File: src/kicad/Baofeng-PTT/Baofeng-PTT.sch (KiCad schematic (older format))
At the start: 18 parts, among them J1 AI, J2 AO, J3 Conn_01x02_Male, J4 PTT, J5 Conn_01x02_Male, J6 Conn_01x02_Male, J7 Conn_01x02_Male, J8 Baofeng, U1 ULN2003

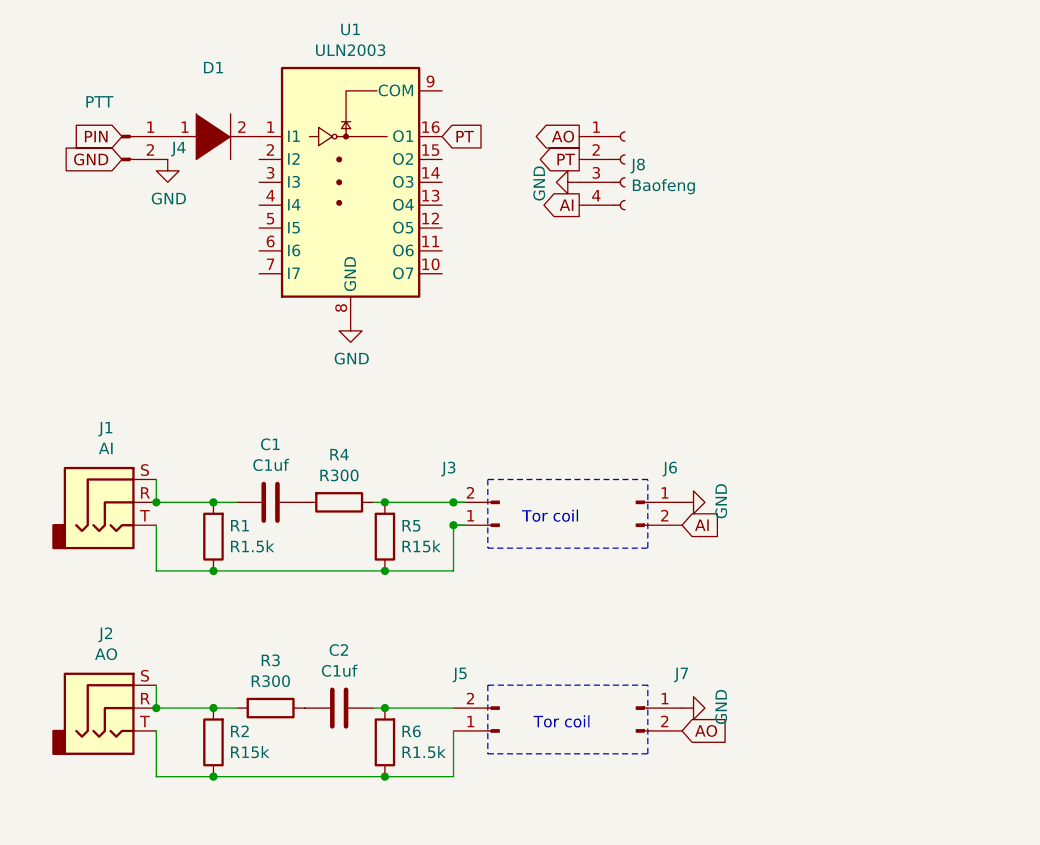
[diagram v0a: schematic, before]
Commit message: Next version of pcb
Reduce size of pcb
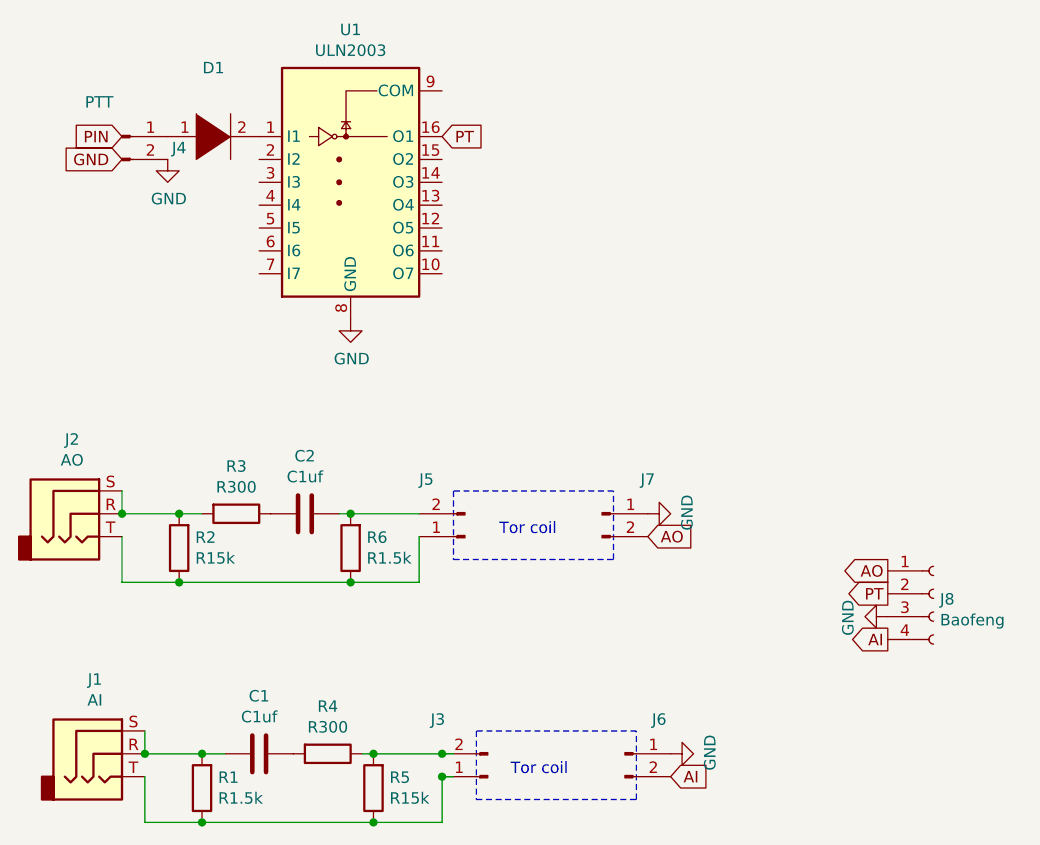
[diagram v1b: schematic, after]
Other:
- moved on the sheet: C1, C2, J1, J2, J3, J5, J6, J7, J8, R1, R2, R3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
